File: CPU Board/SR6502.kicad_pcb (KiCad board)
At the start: 2 copper layers, 127.7 x 120.9 mm, 31 parts, among them J1 Conn_01x40_Female, SW1 RESET, SW2 SWA, SW3 SWA, SW4 SWA, SW5 SWA, SW6 SWA, U2 WD65C02_, U3 74HC00, U4 28C256, U5 CY62256-70PC, U6 WD65C22, U7 WC1602A, X1 1mhz

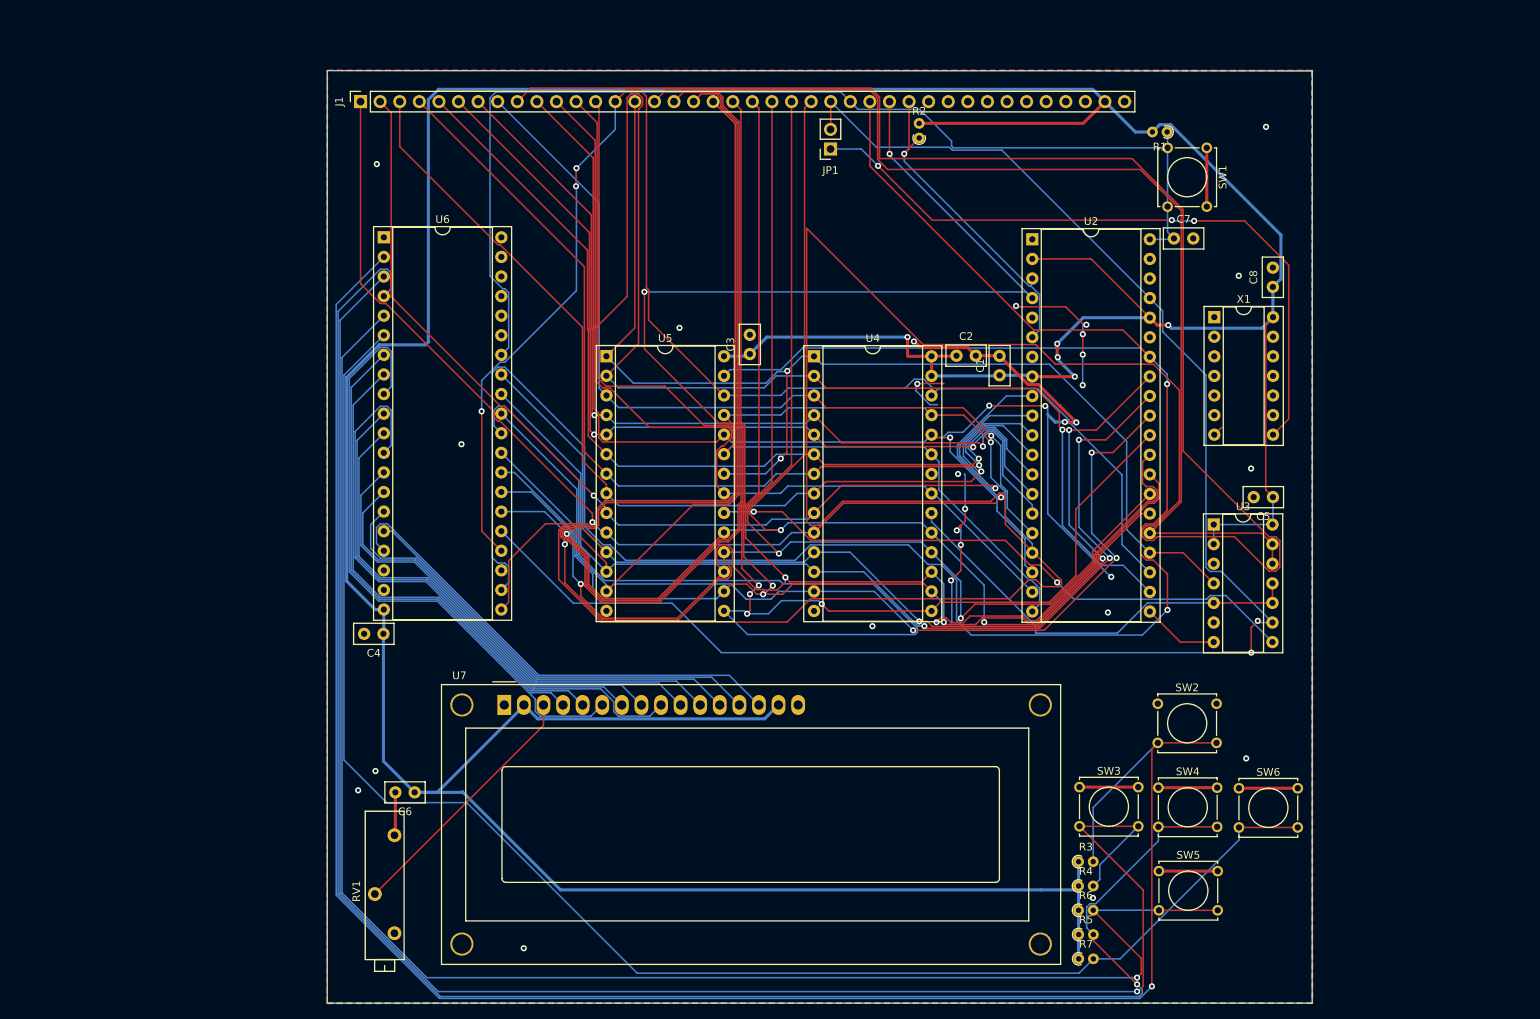
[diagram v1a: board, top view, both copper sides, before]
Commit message: Final push to JLCPCB for latest rev
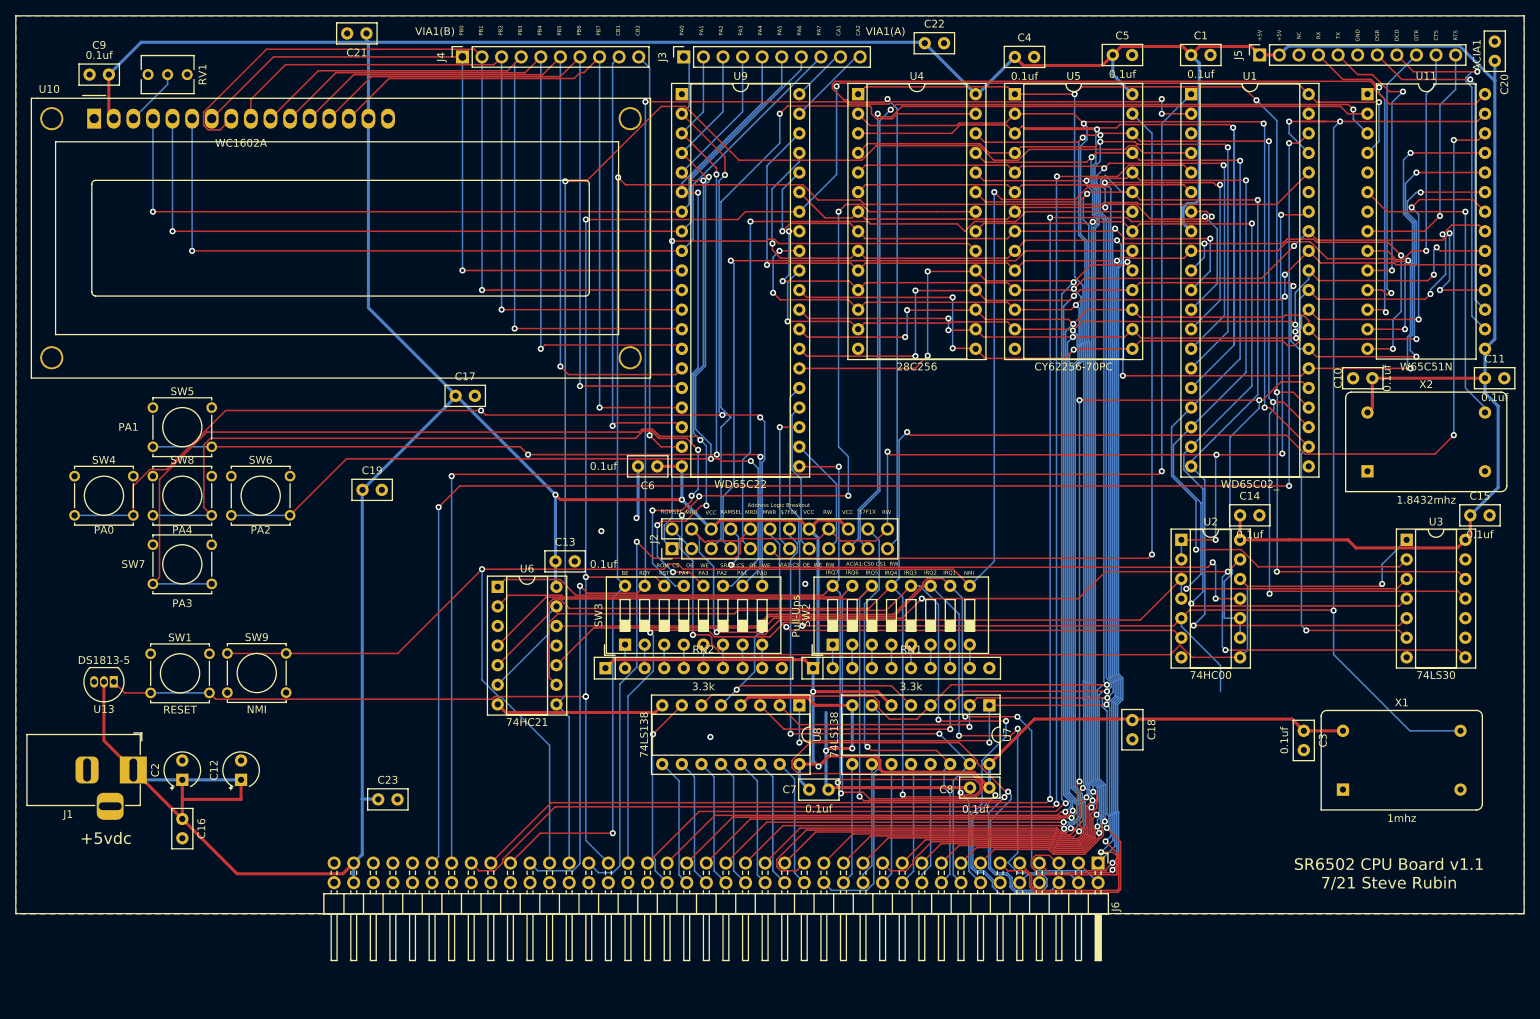
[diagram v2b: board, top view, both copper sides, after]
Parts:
- removed JP1: Jumper, Connector_PinSocket_2.54mm:PinSocket_1x02_P2.54mm_Vertical
- removed R1, R2, R3, R4, R5, R6, R7: 1k, Resistor_THT:R_Axial_DIN0204_L3.6mm_D1.6mm_P1.90mm_Vertical
- added C10: 0.1uf, Capacitor_THT:C_Disc_D5.0mm_W2.5mm_P2.50mm, F.Cu at (215.3, 80.0)
- added C11: 0.1uf, Capacitor_THT:C_Disc_D5.0mm_W2.5mm_P2.50mm, F.Cu at (229.9, 80.0)
- added C12: CP, Capacitor_THT:CP_Radial_Tantal_D4.5mm_P2.50mm, F.Cu at (68.6, 132.1)
- added C13: 0.1uf, Capacitor_THT:C_Disc_D5.0mm_W2.5mm_P2.50mm, F.Cu at (109.3, 103.8)
- added C14: 0.1uf, Capacitor_THT:C_Disc_D5.0mm_W2.5mm_P2.50mm, F.Cu at (198.1, 97.8)
- added C15: 0.1uf, Capacitor_THT:C_Disc_D5.0mm_W2.5mm_P2.50mm, F.Cu at (228.0, 97.8)
- added C16: 0.1uf, Capacitor_THT:C_Disc_D5.0mm_W2.5mm_P2.50mm, F.Cu at (61.0, 137.2)
- added C17: 0.1uf, Capacitor_THT:C_Disc_D5.0mm_W2.5mm_P2.50mm, F.Cu at (96.4, 82.3)
- added C18: 0.1uf, Capacitor_THT:C_Disc_D5.0mm_W2.5mm_P2.50mm, F.Cu at (184.2, 124.3)
- added C19: 0.1uf, Capacitor_THT:C_Disc_D5.0mm_W2.5mm_P2.50mm, F.Cu at (84.3, 94.5)
- added C20: 0.1uf, Capacitor_THT:C_Disc_D5.0mm_W2.5mm_P2.50mm, F.Cu at (231.1, 38.9)
- added C21: 0.1uf, Capacitor_THT:C_Disc_D5.0mm_W2.5mm_P2.50mm, F.Cu at (84.8, 35.3)
- added C22: 0.1uf, Capacitor_THT:C_Disc_D5.0mm_W2.5mm_P2.50mm, F.Cu at (157.2, 36.6)
- added C23: 0.1uf, Capacitor_THT:C_Disc_D5.0mm_W2.5mm_P2.50mm, F.Cu at (86.4, 134.6)
- added C9: 0.1uf, Capacitor_THT:C_Disc_D5.0mm_W2.5mm_P2.50mm, F.Cu at (51.4, 40.6)
- added J2: Conn_02x16_Odd_Even_MountingPin, Connector_PinHeader_2.54mm:PinHeader_2x12_P2.54mm_Vertical, F.Cu at (124.5, 102.1)
- added J3: Conn_01x10_Female, Connector_PinSocket_2.54mm:PinSocket_1x10_P2.54mm_Vertical, F.Cu at (126.0, 38.4)
- added J4: Conn_01x10_Female, Connector_PinSocket_2.54mm:PinSocket_1x10_P2.54mm_Vertical, F.Cu at (97.3, 38.4)
- added J5: ACIA1, Connector_PinSocket_2.54mm:PinSocket_1x11_P2.54mm_Vertical, F.Cu at (200.7, 38.1)
- added J6: Conn_02x40_Female, Connector_PinHeader_2.54mm:PinHeader_2x40_P2.54mm_Horizontal, F.Cu at (179.7, 142.9)
- added RN1: 3.3k, Resistor_THT:R_Array_SIP10, F.Cu at (142.7, 117.6)
- added RN2: 3.3k, Resistor_THT:R_Array_SIP10, F.Cu at (115.8, 117.6)
- added SW7: SW_Push, Button_Switch_THT:SW_Tactile_Straight_KSA0Axx1LFTR, F.Cu at (57.1, 101.6)
- added SW8: SW_Push, Button_Switch_THT:SW_Tactile_Straight_KSA0Axx1LFTR, F.Cu at (57.1, 92.7)
- added SW9: NMI, Button_Switch_THT:SW_Tactile_Straight_KSA0Axx1LFTR, F.Cu at (66.8, 115.7)
- added U1: WD65C02_, Package_DIP:DIP-40_W15.24mm_Socket, F.Cu at (191.8, 43.2)
- added U10: WC1602A, Display:WC1602A, F.Cu at (49.5, 46.4)
- added U11: W65C51N, Package_DIP:DIP-28_W15.24mm, F.Cu at (214.6, 43.2)
- added U13: DS1813-5, Package_TO_SOT_THT:TO-92_Inline, F.Cu at (52.1, 119.4)
- added U8: 74LS138, Package_DIP:DIP-16_W7.62mm_Socket, F.Cu at (141.0, 122.4)
- added U9: WD65C22, Package_DIP:DIP-40_W15.24mm_Socket, F.Cu at (125.7, 43.2)
- added X2: 1.8432mhz, Oscillator:Oscillator_DIP-14, F.Cu at (214.6, 92.1)
- C2: value 0.1uf -> CP; footprint Capacitor_THT:C_Disc_D5.0mm_W2.5mm_P2.50mm -> Capacitor_THT:CP_Radial_Tantal_D4.5mm_P2.50mm
- J1: value Conn_01x40_Female -> 5VDC INPUT; footprint Connector_PinSocket_2.54mm:PinSocket_1x40_P2.54mm_Vertical -> Connector_BarrelJack:BarrelJack_Horizontal
- RV1: footprint Potentiometer_THT:Potentiometer_Vishay_43_Horizontal -> Potentiometer_THT:Potentiometer_Vishay_T73XW_Horizontal
- SW2, SW3: value SWA -> SW_DIP_x08; footprint Button_Switch_THT:SW_Tactile_Straight_KSA0Axx1LFTR -> Button_Switch_THT:SW_DIP_SPSTx08_Slide_9.78x22.5mm_W7.62mm_P2.54mm
- SW4, SW5, SW6: value SWA -> SW_Push
- U2: value WD65C02_ -> 74HC00; footprint Package_DIP:DIP-40_W15.24mm_Socket -> Package_DIP:DIP-14_W7.62mm_Socket
- U3: value 74HC00 -> 74LS30
- U6: value WD65C22 -> 74HC21; footprint Package_DIP:DIP-40_W15.24mm_Socket -> Package_DIP:DIP-14_W7.62mm_Socket
- U7: value WC1602A -> 74LS138; footprint Display:WC1602A -> Package_DIP:DIP-16_W7.62mm_Socket
- X1: footprint Package_DIP:DIP-14_W7.62mm_Socket -> Oscillator:Oscillator_DIP-14
- moved SW1 151.8 mm to (56.9, 115.7), turned to 0 degrees
- moved SW4 146.2 mm to (47.0, 92.7)
- moved SW5 143.6 mm to (57.1, 83.8)
- moved SW6 136.8 mm to (67.3, 92.7)
- moved C2 114.5 mm to (61.0, 132.1), turned to 90 degrees
- moved C4 110.9 mm to (168.9, 38.4), turned to 0 degrees
- moved RV1 102.2 mm to (61.6, 40.6), turned to 270 degrees
- moved J1 91.5 mm to (54.6, 130.8), turned to 0 degrees
- moved C3 86.9 mm to (206.4, 125.7), turned to 270 degrees
- moved C7 85.7 mm to (142.2, 133.3)
- moved C8 74.6 mm to (165.6, 133.1), turned to 180 degrees
- moved X1 63.5 mm to (211.5, 133.3)
- moved U5 62.9 mm to (168.9, 43.2)
- moved U7 62.9 mm to (165.6, 122.4), turned to 270 degrees
- moved SW3 61.8 mm to (118.4, 114.6), turned to 90 degrees
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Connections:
- C7 pad 1: RESET -> VCC
- J1 pad 1: a0 -> VCC
- J1 pad 2: a1 -> GND
- J1 pad 3: a2 -> (no net)
- SW2 pad 1: GND -> Net-(RN1-Pad2)
- SW2 pad 2: B1 -> Net-(RN1-Pad3)
- SW3 pad 1: GND -> Net-(RN2-Pad2)
- SW3 pad 2: B2 -> Net-(RN2-Pad3)
- SW4 pad 2: B3 -> VIA1PA0
- SW5 pad 2: B4 -> VIA1PA1
- SW6 pad 2: B5 -> VIA1PA2
- U2 pad 1: (no net) -> RW
- U2 pad 10: a1 -> a15
- U2 pad 11: a2 -> RAMSEL
- U2 pad 12: a3 -> ROMSEL
- U2 pad 13: a4 -> $7FXX
- U2 pad 14: a5 -> VCC
- U2 pad 2: VCC -> RW
- U2 pad 3: (no net) -> MRD
- U2 pad 4: IRQ -> MRD
- U2 pad 5: (no net) -> PHI2
- U2 pad 6: NMI -> MWR
- U2 pad 7: (no net) -> GND
- U2 pad 8: VCC -> ROMSEL
- U2 pad 9: a0 -> a15
- U3 pad 1: VCC -> ROMSEL
- U3 pad 10: ROM_CS -> (no net)
- U3 pad 11: ROM_CS -> a13
- U3 pad 12: a15 -> a14
- U3 pad 13: a15 -> (no net)
- U3 pad 2: VCC -> a8
- U3 pad 3: (no net) -> a9
- U3 pad 4: a14 -> a10
- U3 pad 5: ROM_CS -> a11
- U3 pad 6: (no net) -> a12
- U3 pad 8: SRAM_CS -> $7FXX
- U3 pad 9: PHI2 -> (no net)
- U4 pad 22: GND -> ROM_OE
- U4 pad 27: VCC -> ROM_WE
- U5 pad 22: a14 -> SRAM_OE
- U5 pad 27: RW -> SRAM_WE
- U6 pad 1: GND -> IRQ7
- U6 pad 10: Net-(U6-Pad10) -> IRQ2
- U6 pad 11: Net-(U6-Pad11) -> (no net)
- U6 pad 12: Net-(U6-Pad12) -> IRQ1
- U6 pad 14: Net-(U6-Pad14) -> VCC
- U6 pad 2: B1 -> IRQ6
- U6 pad 3: B2 -> (no net)
- U6 pad 4: B3 -> IRQ5
- U6 pad 5: B4 -> IRQ4
- U6 pad 6: B5 -> Net-(U6-Pad13)
- U6 pad 7: Net-(U6-Pad7) -> GND
- U6 pad 8: Net-(U6-Pad8) -> IRQ
- U6 pad 9: Net-(U6-Pad9) -> IRQ3
- U7 pad 1: GND -> a4
- U7 pad 10: Net-(U6-Pad13) -> $7F5X
- U7 pad 11: Net-(U6-Pad14) -> $7F4X
- U7 pad 12: Net-(U6-Pad15) -> $7F3X
- U7 pad 13: Net-(U6-Pad16) -> $7F2X
- U7 pad 14: Net-(U6-Pad17) -> $7F1X
- U7 pad 15: VCC -> $7F0X
- U7 pad 16: GND -> VCC
- U7 pad 2: VCC -> a5
- U7 pad 3: Net-(RV1-Pad2) -> a6
- U7 pad 4: Net-(U6-Pad7) -> a7
- U7 pad 5: Net-(U6-Pad8) -> $7FXX
- U7 pad 6: Net-(U6-Pad9) -> VCC
- U7 pad 7: Net-(U6-Pad10) -> $7F7X
- U7 pad 8: Net-(U6-Pad11) -> GND
- U7 pad 9: Net-(U6-Pad12) -> $7F6X
- X1 pad 8: Net-(JP1-Pad1) -> PHI2
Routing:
- net IRQ4: track 0.00 -> 311.0 mm, vias 0 -> 5
- net a8: track 497.1 -> 231.1 mm, vias 1 -> 4
- net B1: track 255.5 -> 0.00 mm, vias 1 -> 0
- net B3: track 234.7 -> 0.00 mm, vias 1 -> 0
- net B2: track 234.0 -> 0.00 mm, vias 1 -> 0
- net VCC: track 563.0 -> 780.2 mm, vias 5 -> 4
- net B4: track 212.4 -> 0.00 mm, vias 1 -> 0
- net SO: track 0.00 -> 205.7 mm, vias 0 -> 3
- net B5: track 201.1 -> 0.00 mm
- net BE: track 0.00 -> 193.9 mm, vias 0 -> 2
- net VP: track 0.00 -> 193.0 mm, vias 0 -> 2
- net READY: track 0.00 -> 188.3 mm, vias 0 -> 4
- net a7: track 112.1 -> 295.4 mm, vias 1 -> 4
- net NMI: track 41.5 -> 223.6 mm, vias 1 -> 2
- net ML: track 0.00 -> 180.0 mm, vias 0 -> 2
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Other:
- board size 127.7 x 120.9 mm -> 195.6 x 116.4 mm
- board text added: "$7F0X"
- board text added: "$7F1X"
- board text added: "+5V"
- board text added: "+5vdc"
- board text added: "ACIA1:CS0 CS1 RW"
- board text added: "Address Logic Breakout"
- board text added: "BE"
- board text added: "CA1"
- board text added: "CA2"
- board text added: "CB1"
- board text added: "CB2"
- board text added: "CTS"
- board text added: "DCD"
- board text added: "DSR"
- board text added: "DTR"
- board text added: "GND"
- board text added: "IRQ1"
- board text added: "IRQ2"
- board text added: "IRQ3"
- board text added: "IRQ4"
- board text added: "IRQ5"
- board text added: "IRQ6"
- board text added: "IRQ7"
- board text added: "MRD"
- board text added: "MWR"
- board text added: "NC"
- board text added: "NMI"
- board text added: "PA0"
- board text added: "PA1"
- board text added: "PA2"
- board text added: "PA3"
- board text added: "PA4"
- board text added: "PA5"
- board text added: "PA6"
- board text added: "PA7"
- board text added: "PB0"
- board text added: "PB1"
- board text added: "PB2"
- board text added: "PB3"
- board text added: "PB4"
- board text added: "PB5"
- board text added: "PB6"
- board text added: "PB7"
- board text added: "Pull-Ups"
- board text added: "RAMSEL"
- board text added: "RDY"
- board text added: "ROM: CS OE WE"
- board text added: "ROMSEL"
- board text added: "RST"
- board text added: "RTS"
- board text added: "RW"
- board text added: "RX"
- board text added: "SR6502 CPU Board v1.1 7/21 Steve Rubin"
- board text added: "SRÅM:CS OE WE"
- board text added: "TX"
- board text added: "VCC"
- board text added: "VIA1(A)"
- board text added: "VIA1(B)"
- board text added: "VIA1:CS OE WE RW"
- board text removed: "SR6502 #1 6/14/2021"
